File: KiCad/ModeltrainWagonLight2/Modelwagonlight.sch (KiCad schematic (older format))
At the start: 17 parts, among them J1 Conn_01x01, J2 Conn_01x01, J3 Conn_01x01, J4 Conn_01x01, U1 LP2951DR

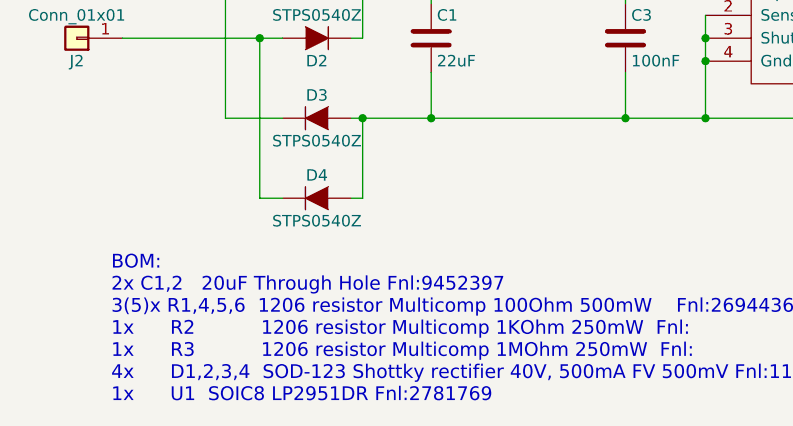
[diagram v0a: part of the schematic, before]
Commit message: Update ModeltrainWagonLight2/Modelwagonlight.sch
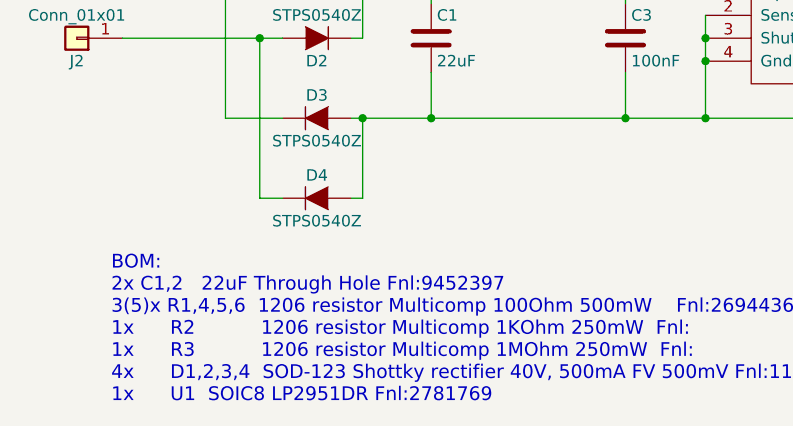
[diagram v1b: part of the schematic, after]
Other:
- note added: "BOM:\n2x C1,2 22uF Through Hole Fnl:9452397\n3(5)x R1,4,5,6 1206 resistor Multicomp 100Ohm 500mW Fnl:2694436\n1x R2 1206 resistor Multicomp 1KOhm 250mW Fnl:\n1x R3 1206 resistor Multicomp 1MOhm 250mW Fnl:\n4x D1,2,3,4 SOD-123 Shottky rectifier 40V, 500mA FV 500mV Fnl:1175677\n1x U1 SOIC8 LP2951DR Fnl:2781769"
- note removed: "BOM:\n2x C1,2 20uF Through Hole Fnl:9452397\n3(5)x R1,4,5,6 1206 resistor Multicomp 100Ohm 500mW Fnl:2694436\n1x R2 1206 resistor Multicomp 1KOhm 250mW Fnl:\n1x R3 1206 resistor Multicomp 1MOhm 250mW Fnl:\n4x D1,2,3,4 SOD-123 Shottky rectifier 40V, 500mA FV 500mV Fnl:1175677\n1x U1 SOIC8 LP2951DR Fnl:2781769"
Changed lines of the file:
@@
 LIBS:switches
 LIBS:relays
-LIBS:motors
 LIBS:transistors
 LIBS:conn
@@
 Connection ~ 5600 4650
 Text Notes 4200 5900 0    60   ~ 0
-BOM:\n2x C1,2   20uF Through Hole Fnl:9452397\n3(5)x R1,4,5,6  1206 resistor Multicomp 100Ohm 500mW    Fnl:2694436\n1x      R2           1206 resistor Multicomp 1KOhm 250mW  Fnl:\n1x      R3           1206 resistor Multicomp 1MOhm 250mW  Fnl:\n4x      D1,2,3,4  SOD-123 Shottky rectifier 40V, 500mA FV 500mV Fnl:1175677\n1x      U1  SOIC8 LP2951DR Fnl:2781769
+BOM:\n2x C1,2   22uF Through Hole Fnl:9452397\n3(5)x R1,4,5,6  1206 resistor Multicomp 100Ohm 500mW    Fnl:2694436\n1x      R2           1206 resistor Multicomp 1KOhm 250mW  Fnl:\n1x      R3           1206 resistor Multicomp 1MOhm 250mW  Fnl:\n4x      D1,2,3,4  SOD-123 Shottky rectifier 40V, 500mA FV 500mV Fnl:1175677\n1x      U1  SOIC8 LP2951DR Fnl:2781769
 $Comp
 L C C1

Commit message: Updated all schematics and layouts. Updated all component lists and csv files. Created ShopCartAll.csv from farnell big order for these 4 boards. Created new gerber files in the board-named directories to be send to PCB farmer.
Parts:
- removed C2: 22uF, Capacitors_THT:CP_Radial_D6.3mm_P2.50mm, symbol C
- removed C4: 100nF, Capacitors_SMD:C_1206, symbol C
- removed D2, D3, D4: STPS0540Z, Diodes_SMD:D_SOD-123, symbol D
- added C2: 22uF, Capacitors_THT:CP_Radial_D6.3mm_P2.50mm, symbol device:CP
- added C4: 100n, Capacitors_SMD:C_1206, symbol device:C
- added D2, D3, D4: STPS0540Z, Diodes_SMD:D_SOD-123, symbol device:D
- C1: symbol C -> device:CP; Farnell (none) -> 9452397; Manufacturer nr (none) -> MCUMHR35V226M6.3X5
- C3: value 100nF -> 100n; symbol C -> device:C; Farnell (none) -> 2896646; Manufacturer nr (none) -> VJ1206Y104KXXPW1BC
- D1: symbol D -> device:D; Farnell (none) -> 1175677; Manufacturer nr (none) -> STPS0540Z
- J1, J2, J3, J4: symbol Conn_01x01 -> Modelwagonlight-rescue:Conn_01x01
- R1: value 10R -> 47E; symbol R -> device:R; Farnell (none) -> 1100156; Manufacturer nr (none) -> WCR1206-47RFI
- R4: value 100R -> 470E; symbol R -> device:R; Farnell (none) -> 1100183; Manufacturer nr (none) -> WCR1206-470RFI
- R5, R6: value 100R -> NP; symbol R -> device:R
- U1: symbol LP2951DR -> LP2951DR-SOIC8:LP2951DR; Farnell (none) -> 2781769; Manufacturer nr (none) -> LP2951DR
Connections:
- wire segments 36 -> 58
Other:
- note added: "02mA --> 1.235V/0.002 = 617 Ohm\n05mA --> 1.235V/0.005 = 247 Ohm\n10mA --> 1.235V/0.010 = 123.5 Ohm\n12mA --> 1.235V/0.012 = 100 Ohm\n15mA --> 1.235V/0.015 = 82.3 Ohm\n20mA --> 1.235V/0.020 = 61.75 Ohm"
- note removed: "05mA --> 1.235V/0.005 = 247 Ohm\n10mA --> 1.235V/0.010 = 123.5 Ohm\n12mA --> 1.235V/0.012 = 100 Ohm\n15mA --> 1.235V/0.015 = 82.3 Ohm\n20mA --> 1.235V/0.020 = 61.75 Ohm"
- note removed: "BOM:\n2x C1,2 22uF Through Hole Fnl:9452397\n3(5)x R1,4,5,6 1206 resistor Multicomp 100Ohm 500mW Fnl:2694436\n1x R2 1206 resistor Multicomp 1KOhm 250mW Fnl:\n1x R3 1206 resistor Multicomp 1MOhm 250mW Fnl:\n4x D1,2,3,4 SOD-123 Shottky rectifier 40V, 500mA FV 500mV Fnl:1175677\n1x U1 SOIC8 LP2951DR Fnl:2781769"
